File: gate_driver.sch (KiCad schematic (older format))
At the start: 7 parts, among them Q7 2N7002, Q8 LBSS84LT1G, Q9 2N7002

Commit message: Connect shutdown and ifsel
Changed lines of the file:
@@
 $Descr A4 11693 8268
 encoding utf-8
-Sheet 4 4
+Sheet 5 6
 Title ""
 Date ""
@@
 AR Path="/60952E6F/60953BA7" Ref="Q9"  Part="1"
 AR Path="/6097174B/60953BA7" Ref="Q?"  Part="1"
-F 0 "Q?" H 3504 4046 50  0000 L CNN
+AR Path="/60B03476/60B1C0DE/60953BA7" Ref="Q9"  Part="1"
+AR Path="/60B03476/60B1C0E2/60953BA7" Ref="Q12"  Part="1"
+F 0 "Q9" H 3504 4046 50  0000 L CNN
 F 1 "2N7002" H 3504 3955 50  0000 L CNN
 F 2 "Package_TO_SOT_SMD:SOT-23" H 3500 3925 50  0001 L CIN
@@
 AR Path="/60952E6F/609545B2" Ref="Q8"  Part="1"
 AR Path="/6097174B/609545B2" Ref="Q?"  Part="1"
-F 0 "Q?" H 3505 3154 50  0000 L CNN
+AR Path="/60B03476/60B1C0DE/609545B2" Ref="Q8"  Part="1"
+AR Path="/60B03476/60B1C0E2/609545B2" Ref="Q11"  Part="1"
+F 0 "Q8" H 3505 3154 50  0000 L CNN
 F 1 "LBSS84LT1G" H 3505 3245 50  0000 L CNN
 F 2 "Package_TO_SOT_SMD:SOT-23" H 3500 3300 50  0001 C CNN
@@
 AR Path="/60952E6F/60954F7A" Ref="R15"  Part="1"
 AR Path="/6097174B/60954F7A" Ref="R?"  Part="1"
-F 0 "R?" V 3393 3550 50  0000 C CNN
+AR Path="/60B03476/60B1C0DE/60954F7A" Ref="R17"  Part="1"
+AR Path="/60B03476/60B1C0E2/60954F7A" Ref="R21"  Part="1"
+F 0 "R17" V 3393 3550 50  0000 C CNN
 F 1 "33R" V 3484 3550 50  0000 C CNN
 F 2 "Resistor_SMD:R_0603_1608Metric" V 3530 3550 50  0001 C CNN
@@
 AR Path="/60952E6F/609554C2" Ref="R16"  Part="1"
 AR Path="/6097174B/609554C2" Ref="R?"  Part="1"
-F 0 "R?" V 3500 3750 50  0000 C CNN
+AR Path="/60B03476/60B1C0DE/609554C2" Ref="R18"  Part="1"
+AR Path="/60B03476/60B1C0E2/609554C2" Ref="R22"  Part="1"
+F 0 "R18" V 3500 3750 50  0000 C CNN
 F 1 "33R" V 3700 3750 50  0000 C CNN
 F 2 "Resistor_SMD:R_0603_1608Metric" V 3530 3750 50  0001 C CNN
@@
 AR Path="/60952E6F/6095D3BF" Ref="Q7"  Part="1"
 AR Path="/6097174B/6095D3BF" Ref="Q?"  Part="1"
-F 0 "Q?" H 2704 3846 50  0000 L CNN
+AR Path="/60B03476/60B1C0DE/6095D3BF" Ref="Q7"  Part="1"
+AR Path="/60B03476/60B1C0E2/6095D3BF" Ref="Q10"  Part="1"
+F 0 "Q7" H 2704 3846 50  0000 L CNN
 F 1 "2N7002" H 2704 3755 50  0000 L CNN
 F 2 "Package_TO_SOT_SMD:SOT-23" H 2700 3725 50  0001 L CIN
@@
 AR Path="/60952E6F/60962EC9" Ref="R14"  Part="1"
 AR Path="/6097174B/60962EC9" Ref="R?"  Part="1"
-F 0 "R?" V 2393 3150 50  0000 C CNN
+AR Path="/60B03476/60B1C0DE/60962EC9" Ref="R16"  Part="1"
+AR Path="/60B03476/60B1C0E2/60962EC9" Ref="R20"  Part="1"
+F 0 "R16" V 2393 3150 50  0000 C CNN
 F 1 "1kR" V 2484 3150 50  0000 C CNN
 F 2 "Resistor_SMD:R_0402_1005Metric" V 2530 3150 50  0001 C CNN
@@
 AR Path="/60952E6F/609638C0" Ref="#PWR0138"  Part="1"
 AR Path="/6097174B/609638C0" Ref="#PWR?"  Part="1"
-F 0 "#PWR?" H 2600 2750 50  0001 C CNN
+AR Path="/60B03476/60B1C0DE/609638C0" Ref="#PWR0151"  Part="1"
+AR Path="/60B03476/60B1C0E2/609638C0" Ref="#PWR0153"  Part="1"
+F 0 "#PWR0151" H 2600 2750 50  0001 C CNN
 F 1 "+5V" H 2615 3073 50  0000 C CNN
 F 2 "" H 2600 2900 50  0001 C CNN
@@
 AR Path="/60952E6F/609649C8" Ref="#PWR0139"  Part="1"
 AR Path="/6097174B/609649C8" Ref="#PWR?"  Part="1"
-F 0 "#PWR?" H 2600 4050 50  0001 C CNN
+AR Path="/60B03476/60B1C0DE/609649C8" Ref="#PWR0152"  Part="1"
+AR Path="/60B03476/60B1C0E2/609649C8" Ref="#PWR0154"  Part="1"
+F 0 "#PWR0152" H 2600 4050 50  0001 C CNN
 F 1 "GND" H 2605 4127 50  0000 C CNN
 F 2 "" H 2600 4300 50  0001 C CNN
@@
 AR Path="/60952E6F/60968798" Ref="R13"  Part="1"
 AR Path="/6097174B/60968798" Ref="R?"  Part="1"
-F 0 "R?" H 2320 4096 50  0000 L CNN
+AR Path="/60B03476/60B1C0DE/60968798" Ref="R15"  Part="1"
+AR Path="/60B03476/60B1C0E2/60968798" Ref="R19"  Part="1"
+F 0 "R15" H 2320 4096 50  0000 L CNN
 F 1 "100kR" H 2320 4005 50  0000 L CNN
 F 2 "Resistor_SMD:R_0402_1005Metric" V 2180 4050 50  0001 C CNN

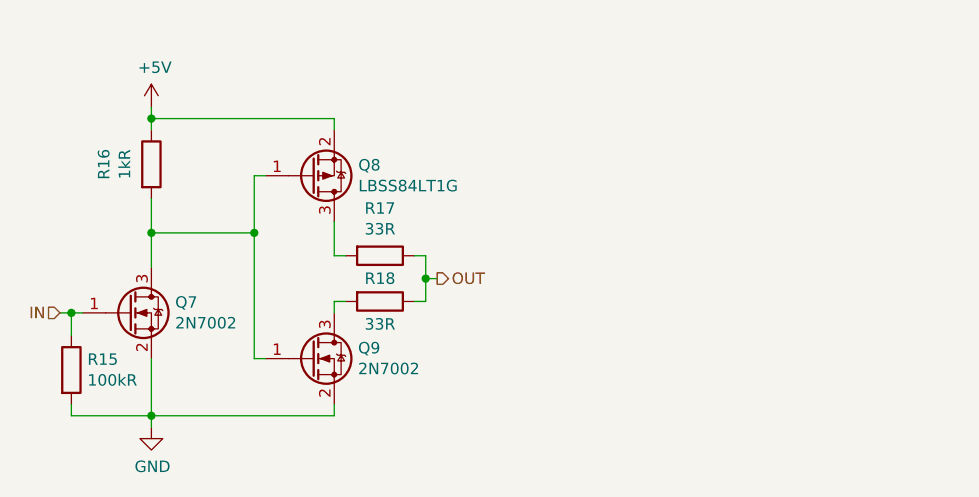
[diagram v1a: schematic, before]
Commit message: Add VFD section
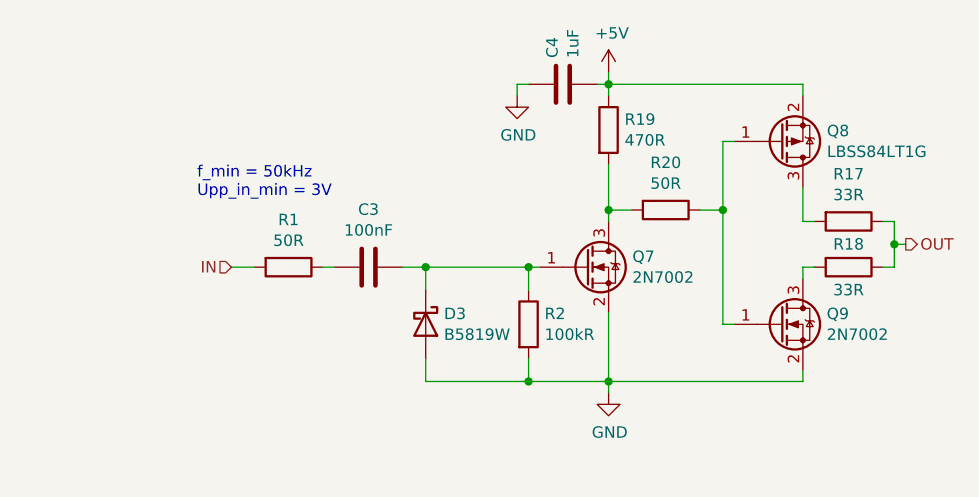
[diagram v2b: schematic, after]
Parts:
- removed R13: 100kR, Resistor_SMD:R_0402_1005Metric, symbol Device:R
- removed R14: 1kR, Resistor_SMD:R_0402_1005Metric, symbol Device:R
- added C3: 100nF, Capacitor_SMD:C_0402_1005Metric, symbol Device:C
- added C4: 1uF, Capacitor_SMD:C_0402_1005Metric, symbol Device:C
- added D3: B5819W, Diode_SMD:D_SOD-123, symbol Device:D_Schottky
- added R1, R20: 50R, Resistor_SMD:R_0402_1005Metric, symbol Device:R
- added R19: 470R, Resistor_SMD:R_0402_1005Metric, symbol Device:R
- added R2: 100kR, Resistor_SMD:R_0402_1005Metric, symbol Device:R
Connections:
- net +5V: now also C4.2, R19.1
- net GND: now also C4.1, D3.2 (A), R2.2
- net IN: now also R1.2; no longer Q7.1 (G)
- net at Q8.1 (G), Q9.1 (G): now also R20.1; no longer Q7.3 (D)
- new net: Q7.3 (D), R19.2, R20.2
- new net: C3.1, D3.1 (K), Q7.1 (G), R2.1
- new net: C3.2, R1.1
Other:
- note added: "f_min = 50kHz\nUpp_in_min = 3V"
- moved on the sheet: Q8, Q9, R17, R18

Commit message: Complete intra section layout
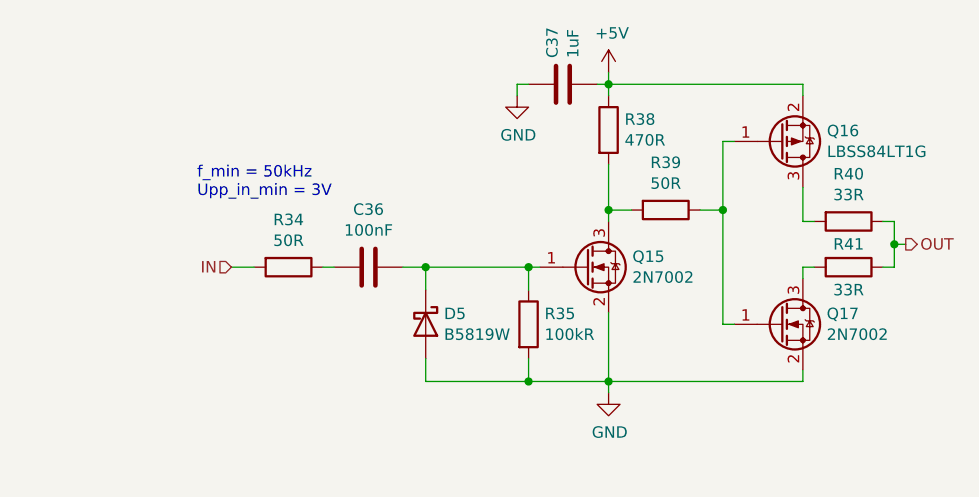
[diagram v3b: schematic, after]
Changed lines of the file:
@@
 $Descr A4 11693 8268
 encoding utf-8
-Sheet 5 7
+Sheet 7 7
 Title ""
 Date ""
@@
 AR Path="/60B03476/60B1C0E2/60953BA7" Ref="Q12"  Part="1"
 AR Path="/60B03476/6147410E/60953BA7" Ref="Q17"  Part="1"
-F 0 "Q9" H 5554 3896 50  0000 L CNN
+F 0 "Q17" H 5554 3896 50  0000 L CNN
 F 1 "2N7002" H 5554 3805 50  0000 L CNN
 F 2 "Package_TO_SOT_SMD:SOT-23" H 5550 3775 50  0001 L CIN
@@
 AR Path="/60B03476/60B1C0E2/609545B2" Ref="Q11"  Part="1"
 AR Path="/60B03476/6147410E/609545B2" Ref="Q16"  Part="1"
-F 0 "Q8" H 5555 3004 50  0000 L CNN
+F 0 "Q16" H 5555 3004 50  0000 L CNN
 F 1 "LBSS84LT1G" H 5555 3095 50  0000 L CNN
 F 2 "Package_TO_SOT_SMD:SOT-23" H 5550 3150 50  0001 C CNN
@@
 AR Path="/60B03476/60B1C0E2/60954F7A" Ref="R21"  Part="1"
 AR Path="/60B03476/6147410E/60954F7A" Ref="R40"  Part="1"
-F 0 "R17" V 5443 3400 50  0000 C CNN
+F 0 "R40" V 5443 3400 50  0000 C CNN
 F 1 "33R" V 5534 3400 50  0000 C CNN
 F 2 "Resistor_SMD:R_0603_1608Metric" V 5580 3400 50  0001 C CNN
@@
 AR Path="/60B03476/60B1C0E2/609554C2" Ref="R22"  Part="1"
 AR Path="/60B03476/6147410E/609554C2" Ref="R41"  Part="1"
-F 0 "R18" V 5550 3600 50  0000 C CNN
+F 0 "R41" V 5550 3600 50  0000 C CNN
 F 1 "33R" V 5750 3600 50  0000 C CNN
 F 2 "Resistor_SMD:R_0603_1608Metric" V 5580 3600 50  0001 C CNN
@@
 AR Path="/60B03476/60B1C0E2/609638C0" Ref="#PWR0153"  Part="1"
 AR Path="/60B03476/6147410E/609638C0" Ref="#PWR0169"  Part="1"
-F 0 "#PWR0151" H 4600 2600 50  0001 C CNN
+F 0 "#PWR0169" H 4600 2600 50  0001 C CNN
 F 1 "+5V" H 4615 2923 50  0000 C CNN
 F 2 "" H 4600 2750 50  0001 C CNN
@@
 AR Path="/60B03476/60B1C0E2/609649C8" Ref="#PWR0154"  Part="1"
 AR Path="/60B03476/6147410E/609649C8" Ref="#PWR0170"  Part="1"
-F 0 "#PWR0152" H 4600 3900 50  0001 C CNN
+F 0 "#PWR0170" H 4600 3900 50  0001 C CNN
 F 1 "GND" H 4605 3977 50  0000 C CNN
 F 2 "" H 4600 4150 50  0001 C CNN
@@
 AR Path="/60B03476/60B1C0E2/613423AB" Ref="R37"  Part="1"
 AR Path="/60B03476/6147410E/613423AB" Ref="R39"  Part="1"
-F 0 "R20" V 4643 3350 50  0000 C CNN
+F 0 "R39" V 4643 3350 50  0000 C CNN
 F 1 "50R" V 4734 3350 50  0000 C CNN
 F 2 "Resistor_SMD:R_0402_1005Metric" V 4780 3350 50  0001 C CNN
@@
 AR Path="/60B03476/60B1C0E2/61342809" Ref="R36"  Part="1"
 AR Path="/60B03476/6147410E/61342809" Ref="R38"  Part="1"
-F 0 "R19" H 4670 3046 50  0000 L CNN
+F 0 "R38" H 4670 3046 50  0000 L CNN
 F 1 "470R" H 4670 2955 50  0000 L CNN
 F 2 "Resistor_SMD:R_0402_1005Metric" V 4530 3000 50  0001 C CNN
@@
 AR Path="/60B03476/60B1C0E2/6134758B" Ref="C33"  Part="1"
 AR Path="/60B03476/6147410E/6134758B" Ref="C37"  Part="1"
-F 0 "C4" H 4515 2846 50  0000 L CNN
+F 0 "C37" H 4515 2846 50  0000 L CNN
 F 1 "1uF" H 4515 2755 50  0000 L CNN
 F 2 "Capacitor_SMD:C_0402_1005Metric" H 4438 2650 50  0001 C CNN
@@
 AR Path="/60B03476/60B1C0E2/61347A56" Ref="#PWR0165"  Part="1"
 AR Path="/60B03476/6147410E/61347A56" Ref="#PWR0171"  Part="1"
-F 0 "#PWR0164" H 4200 2600 50  0001 C CNN
+F 0 "#PWR0171" H 4200 2600 50  0001 C CNN
 F 1 "GND" H 4205 2677 50  0000 C CNN
 F 2 "" H 4200 2850 50  0001 C CNN
@@
 AR Path="/60B03476/60B1C0E2/61362E0C" Ref="Q10"  Part="1"
 AR Path="/60B03476/6147410E/61362E0C" Ref="Q15"  Part="1"
-F 0 "Q7" H 4704 3646 50  0000 L CNN
+F 0 "Q15" H 4704 3646 50  0000 L CNN
 F 1 "2N7002" H 4704 3555 50  0000 L CNN
 F 2 "Package_TO_SOT_SMD:SOT-23" H 4700 3525 50  0001 L CIN
@@
 AR Path="/60B03476/60B1C0E2/613656C0" Ref="R15"  Part="1"
 AR Path="/60B03476/6147410E/613656C0" Ref="R34"  Part="1"
-F 0 "R1" V 2993 3600 50  0000 C CNN
+F 0 "R34" V 2993 3600 50  0000 C CNN
 F 1 "50R" V 3084 3600 50  0000 C CNN
 F 2 "Resistor_SMD:R_0402_1005Metric" V 3130 3600 50  0001 C CNN
@@
 AR Path="/60B03476/60B1C0E2/61381B15" Ref="R16"  Part="1"
 AR Path="/60B03476/6147410E/61381B15" Ref="R35"  Part="1"
-F 0 "R2" H 4320 3896 50  0000 L CNN
+F 0 "R35" H 4320 3896 50  0000 L CNN
 F 1 "100kR" H 4320 3805 50  0000 L CNN
 F 2 "Resistor_SMD:R_0402_1005Metric" V 4180 3850 50  0001 C CNN
@@
 AR Path="/60B03476/60B1C0E2/6138763F" Ref="C32"  Part="1"
 AR Path="/60B03476/6147410E/6138763F" Ref="C36"  Part="1"
-F 0 "C3" V 3298 3600 50  0000 C CNN
+F 0 "C36" V 3298 3600 50  0000 C CNN
 F 1 "100nF" V 3389 3600 50  0000 C CNN
 F 2 "Capacitor_SMD:C_0402_1005Metric" H 3588 3450 50  0001 C CNN
@@
 AR Path="/60B03476/60B1C0E2/6135A9B7" Ref="D4"  Part="1"
 AR Path="/60B03476/6147410E/6135A9B7" Ref="D5"  Part="1"
-F 0 "D3" V 3754 3930 50  0000 L CNN
+F 0 "D5" V 3754 3930 50  0000 L CNN
 F 1 "B5819W" V 3845 3930 50  0000 L CNN
 F 2 "Diode_SMD:D_SOD-123" H 3800 3850 50  0001 C CNN

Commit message: Add missing LCSC partnumbers
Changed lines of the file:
@@
 $Descr A4 11693 8268
 encoding utf-8
-Sheet 7 7
+Sheet 5 7
 Title ""
 Date ""
@@
 AR Path="/60B03476/60B1C0E2/60953BA7" Ref="Q12"  Part="1"
 AR Path="/60B03476/6147410E/60953BA7" Ref="Q17"  Part="1"
-F 0 "Q17" H 5554 3896 50  0000 L CNN
+F 0 "Q9" H 5554 3896 50  0000 L CNN
 F 1 "2N7002" H 5554 3805 50  0000 L CNN
 F 2 "Package_TO_SOT_SMD:SOT-23" H 5550 3775 50  0001 L CIN
@@
 AR Path="/60B03476/60B1C0E2/609545B2" Ref="Q11"  Part="1"
 AR Path="/60B03476/6147410E/609545B2" Ref="Q16"  Part="1"
-F 0 "Q16" H 5555 3004 50  0000 L CNN
+F 0 "Q8" H 5555 3004 50  0000 L CNN
 F 1 "LBSS84LT1G" H 5555 3095 50  0000 L CNN
 F 2 "Package_TO_SOT_SMD:SOT-23" H 5550 3150 50  0001 C CNN
@@
 AR Path="/60B03476/60B1C0E2/60954F7A" Ref="R21"  Part="1"
 AR Path="/60B03476/6147410E/60954F7A" Ref="R40"  Part="1"
-F 0 "R40" V 5443 3400 50  0000 C CNN
+F 0 "R17" V 5443 3400 50  0000 C CNN
 F 1 "33R" V 5534 3400 50  0000 C CNN
 F 2 "Resistor_SMD:R_0603_1608Metric" V 5580 3400 50  0001 C CNN
@@
 AR Path="/60B03476/60B1C0E2/609554C2" Ref="R22"  Part="1"
 AR Path="/60B03476/6147410E/609554C2" Ref="R41"  Part="1"
-F 0 "R41" V 5550 3600 50  0000 C CNN
+F 0 "R18" V 5550 3600 50  0000 C CNN
 F 1 "33R" V 5750 3600 50  0000 C CNN
 F 2 "Resistor_SMD:R_0603_1608Metric" V 5580 3600 50  0001 C CNN
@@
 AR Path="/60B03476/60B1C0E2/613423AB" Ref="R37"  Part="1"
 AR Path="/60B03476/6147410E/613423AB" Ref="R39"  Part="1"
-F 0 "R39" V 4643 3350 50  0000 C CNN
+F 0 "R20" V 4643 3350 50  0000 C CNN
 F 1 "50R" V 4734 3350 50  0000 C CNN
 F 2 "Resistor_SMD:R_0402_1005Metric" V 4780 3350 50  0001 C CNN
@@
 AR Path="/60B03476/60B1C0E2/61342809" Ref="R36"  Part="1"
 AR Path="/60B03476/6147410E/61342809" Ref="R38"  Part="1"
-F 0 "R38" H 4670 3046 50  0000 L CNN
+F 0 "R19" H 4670 3046 50  0000 L CNN
 F 1 "470R" H 4670 2955 50  0000 L CNN
 F 2 "Resistor_SMD:R_0402_1005Metric" V 4530 3000 50  0001 C CNN
@@
 AR Path="/60B03476/60B1C0E2/6134758B" Ref="C33"  Part="1"
 AR Path="/60B03476/6147410E/6134758B" Ref="C37"  Part="1"
-F 0 "C37" H 4515 2846 50  0000 L CNN
+F 0 "C4" H 4515 2846 50  0000 L CNN
 F 1 "1uF" H 4515 2755 50  0000 L CNN
 F 2 "Capacitor_SMD:C_0402_1005Metric" H 4438 2650 50  0001 C CNN
@@
 AR Path="/60B03476/60B1C0E2/61362E0C" Ref="Q10"  Part="1"
 AR Path="/60B03476/6147410E/61362E0C" Ref="Q15"  Part="1"
-F 0 "Q15" H 4704 3646 50  0000 L CNN
+F 0 "Q7" H 4704 3646 50  0000 L CNN
 F 1 "2N7002" H 4704 3555 50  0000 L CNN
 F 2 "Package_TO_SOT_SMD:SOT-23" H 4700 3525 50  0001 L CIN
@@
 AR Path="/60B03476/60B1C0E2/613656C0" Ref="R15"  Part="1"
 AR Path="/60B03476/6147410E/613656C0" Ref="R34"  Part="1"
-F 0 "R34" V 2993 3600 50  0000 C CNN
+F 0 "R1" V 2993 3600 50  0000 C CNN
 F 1 "50R" V 3084 3600 50  0000 C CNN
 F 2 "Resistor_SMD:R_0402_1005Metric" V 3130 3600 50  0001 C CNN
@@
 AR Path="/60B03476/60B1C0E2/61381B15" Ref="R16"  Part="1"
 AR Path="/60B03476/6147410E/61381B15" Ref="R35"  Part="1"
-F 0 "R35" H 4320 3896 50  0000 L CNN
+F 0 "R2" H 4320 3896 50  0000 L CNN
 F 1 "100kR" H 4320 3805 50  0000 L CNN
 F 2 "Resistor_SMD:R_0402_1005Metric" V 4180 3850 50  0001 C CNN
@@
 AR Path="/60B03476/60B1C0E2/6138763F" Ref="C32"  Part="1"
 AR Path="/60B03476/6147410E/6138763F" Ref="C36"  Part="1"
-F 0 "C36" V 3298 3600 50  0000 C CNN
+F 0 "C3" V 3298 3600 50  0000 C CNN
 F 1 "100nF" V 3389 3600 50  0000 C CNN
 F 2 "Capacitor_SMD:C_0402_1005Metric" H 3588 3450 50  0001 C CNN
@@
 AR Path="/60B03476/60B1C0E2/6135A9B7" Ref="D4"  Part="1"
 AR Path="/60B03476/6147410E/6135A9B7" Ref="D5"  Part="1"
-F 0 "D5" V 3754 3930 50  0000 L CNN
+F 0 "D3" V 3754 3930 50  0000 L CNN
 F 1 "B5819W" V 3845 3930 50  0000 L CNN
 F 2 "Diode_SMD:D_SOD-123" H 3800 3850 50  0001 C CNN

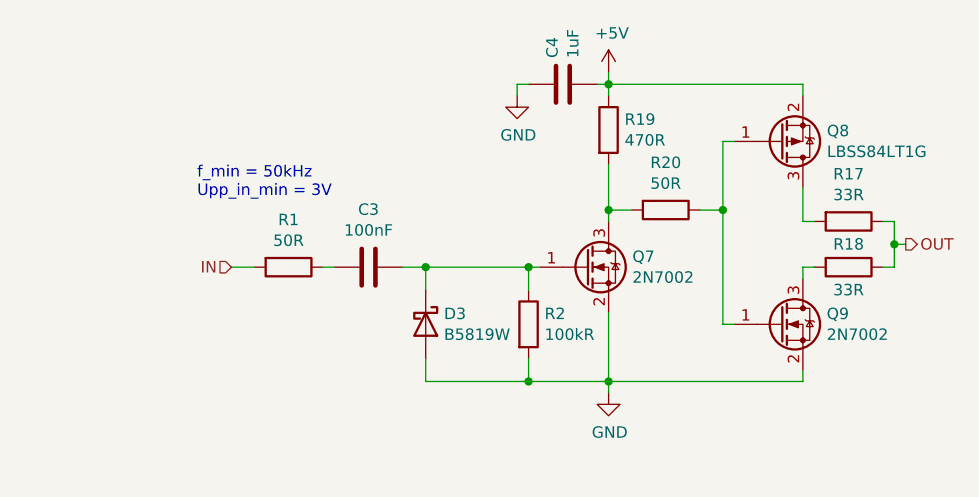
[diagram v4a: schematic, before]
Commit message: Add additional VFD VDD2 bulk capacitance
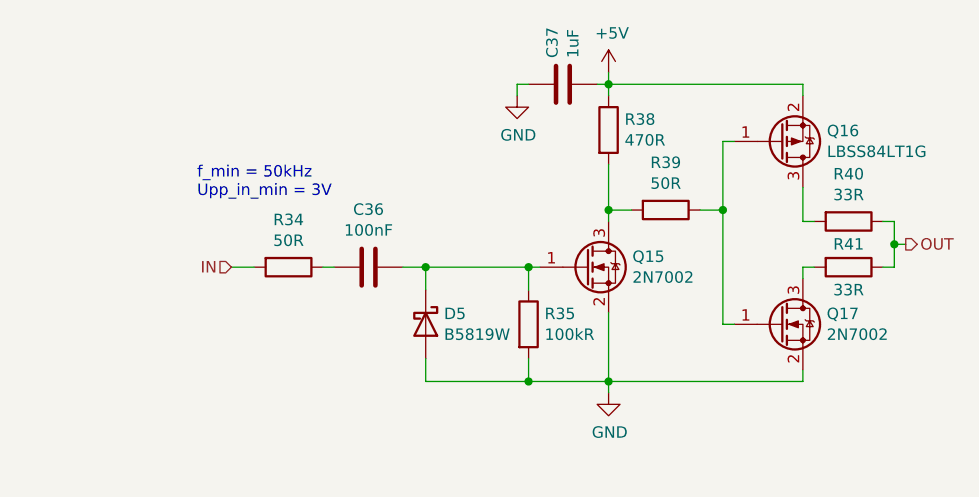
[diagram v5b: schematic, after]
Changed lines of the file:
@@
 AR Path="/60B03476/60B1C0E2/60953BA7" Ref="Q12"  Part="1"
 AR Path="/60B03476/6147410E/60953BA7" Ref="Q17"  Part="1"
-F 0 "Q9" H 5554 3896 50  0000 L CNN
+F 0 "Q17" H 5554 3896 50  0000 L CNN
 F 1 "2N7002" H 5554 3805 50  0000 L CNN
 F 2 "Package_TO_SOT_SMD:SOT-23" H 5550 3775 50  0001 L CIN
@@
 AR Path="/60B03476/60B1C0E2/609545B2" Ref="Q11"  Part="1"
 AR Path="/60B03476/6147410E/609545B2" Ref="Q16"  Part="1"
-F 0 "Q8" H 5555 3004 50  0000 L CNN
+F 0 "Q16" H 5555 3004 50  0000 L CNN
 F 1 "LBSS84LT1G" H 5555 3095 50  0000 L CNN
 F 2 "Package_TO_SOT_SMD:SOT-23" H 5550 3150 50  0001 C CNN
@@
 AR Path="/60B03476/60B1C0E2/60954F7A" Ref="R21"  Part="1"
 AR Path="/60B03476/6147410E/60954F7A" Ref="R40"  Part="1"
-F 0 "R17" V 5443 3400 50  0000 C CNN
+F 0 "R40" V 5443 3400 50  0000 C CNN
 F 1 "33R" V 5534 3400 50  0000 C CNN
 F 2 "Resistor_SMD:R_0603_1608Metric" V 5580 3400 50  0001 C CNN
@@
 AR Path="/60B03476/60B1C0E2/609554C2" Ref="R22"  Part="1"
 AR Path="/60B03476/6147410E/609554C2" Ref="R41"  Part="1"
-F 0 "R18" V 5550 3600 50  0000 C CNN
+F 0 "R41" V 5550 3600 50  0000 C CNN
 F 1 "33R" V 5750 3600 50  0000 C CNN
 F 2 "Resistor_SMD:R_0603_1608Metric" V 5580 3600 50  0001 C CNN
@@
 AR Path="/60B03476/60B1C0E2/613423AB" Ref="R37"  Part="1"
 AR Path="/60B03476/6147410E/613423AB" Ref="R39"  Part="1"
-F 0 "R20" V 4643 3350 50  0000 C CNN
+F 0 "R39" V 4643 3350 50  0000 C CNN
 F 1 "50R" V 4734 3350 50  0000 C CNN
 F 2 "Resistor_SMD:R_0402_1005Metric" V 4780 3350 50  0001 C CNN
@@
 AR Path="/60B03476/60B1C0E2/61342809" Ref="R36"  Part="1"
 AR Path="/60B03476/6147410E/61342809" Ref="R38"  Part="1"
-F 0 "R19" H 4670 3046 50  0000 L CNN
+F 0 "R38" H 4670 3046 50  0000 L CNN
 F 1 "470R" H 4670 2955 50  0000 L CNN
 F 2 "Resistor_SMD:R_0402_1005Metric" V 4530 3000 50  0001 C CNN
@@
 AR Path="/60B03476/60B1C0E2/6134758B" Ref="C33"  Part="1"
 AR Path="/60B03476/6147410E/6134758B" Ref="C37"  Part="1"
-F 0 "C4" H 4515 2846 50  0000 L CNN
+F 0 "C37" H 4515 2846 50  0000 L CNN
 F 1 "1uF" H 4515 2755 50  0000 L CNN
 F 2 "Capacitor_SMD:C_0402_1005Metric" H 4438 2650 50  0001 C CNN
@@
 AR Path="/60B03476/60B1C0E2/61362E0C" Ref="Q10"  Part="1"
 AR Path="/60B03476/6147410E/61362E0C" Ref="Q15"  Part="1"
-F 0 "Q7" H 4704 3646 50  0000 L CNN
+F 0 "Q15" H 4704 3646 50  0000 L CNN
 F 1 "2N7002" H 4704 3555 50  0000 L CNN
 F 2 "Package_TO_SOT_SMD:SOT-23" H 4700 3525 50  0001 L CIN
@@
 AR Path="/60B03476/60B1C0E2/613656C0" Ref="R15"  Part="1"
 AR Path="/60B03476/6147410E/613656C0" Ref="R34"  Part="1"
-F 0 "R1" V 2993 3600 50  0000 C CNN
+F 0 "R34" V 2993 3600 50  0000 C CNN
 F 1 "50R" V 3084 3600 50  0000 C CNN
 F 2 "Resistor_SMD:R_0402_1005Metric" V 3130 3600 50  0001 C CNN
@@
 AR Path="/60B03476/60B1C0E2/61381B15" Ref="R16"  Part="1"
 AR Path="/60B03476/6147410E/61381B15" Ref="R35"  Part="1"
-F 0 "R2" H 4320 3896 50  0000 L CNN
+F 0 "R35" H 4320 3896 50  0000 L CNN
 F 1 "100kR" H 4320 3805 50  0000 L CNN
 F 2 "Resistor_SMD:R_0402_1005Metric" V 4180 3850 50  0001 C CNN
@@
 AR Path="/60B03476/60B1C0E2/6138763F" Ref="C32"  Part="1"
 AR Path="/60B03476/6147410E/6138763F" Ref="C36"  Part="1"
-F 0 "C3" V 3298 3600 50  0000 C CNN
+F 0 "C36" V 3298 3600 50  0000 C CNN
 F 1 "100nF" V 3389 3600 50  0000 C CNN
 F 2 "Capacitor_SMD:C_0402_1005Metric" H 3588 3450 50  0001 C CNN
@@
 AR Path="/60B03476/60B1C0E2/6135A9B7" Ref="D4"  Part="1"
 AR Path="/60B03476/6147410E/6135A9B7" Ref="D5"  Part="1"
-F 0 "D3" V 3754 3930 50  0000 L CNN
+F 0 "D5" V 3754 3930 50  0000 L CNN
 F 1 "B5819W" V 3845 3930 50  0000 L CNN
 F 2 "Diode_SMD:D_SOD-123" H 3800 3850 50  0001 C CNN
